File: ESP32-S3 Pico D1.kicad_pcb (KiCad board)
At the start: 6 copper layers, 31 x 30.5 mm, 55 parts, among them CN1 USC_C_Receptacle_Hirose_CX90M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, CN2 BM04B-ACHSS, CN3 Conn_Coaxial_Small, SW1 SPST-NO, SW2 SPST-NO, U1 TPSM82903, U2 TPS2117DRL, U3 TPS2117DRL, U4 NCP167, U5 ESP32-S3-PICO-1-N8R8, U6 BGS12WN6, U7 TCAN1057AVDRBRQ1, U8 74HCT00

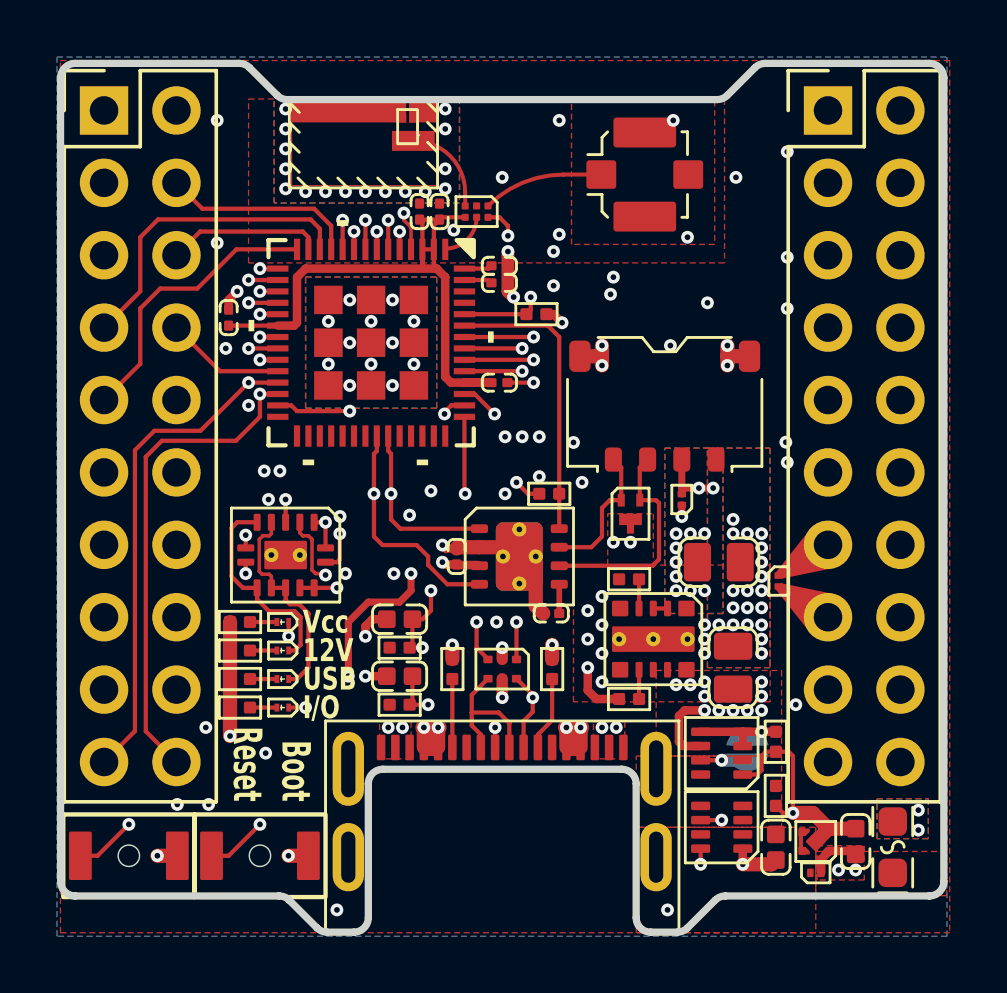
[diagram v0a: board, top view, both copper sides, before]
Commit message: successful 1st pass, but I want to try some new bus'ing techniques to clean up the routing
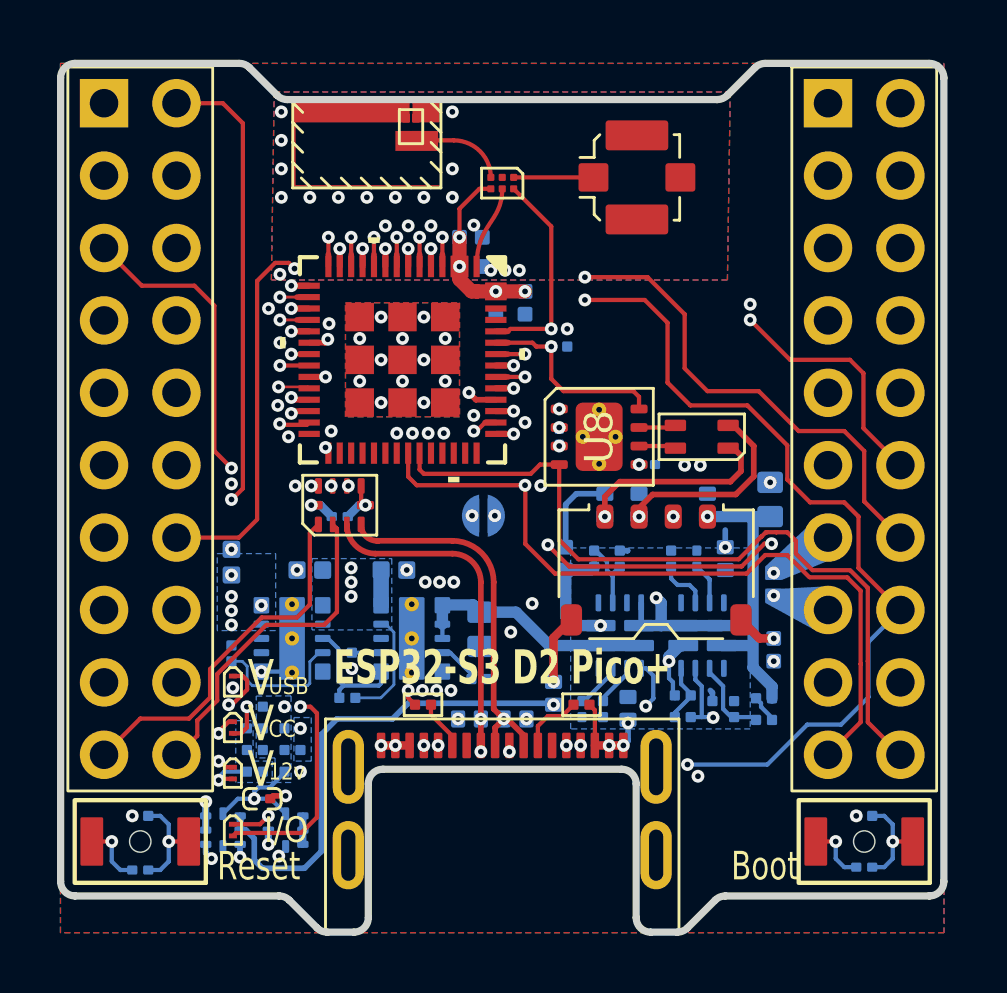
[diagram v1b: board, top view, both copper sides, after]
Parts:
- removed C13: 100n, Capacitors:C0201_Dense
- removed ESD1: PRTR5V0U2F, Personal_FootprintLibrary:XSON6
- removed ESD2: ESDCAN03-2BM3Y, Personal_FootprintLibrary:DFN1110-3
- removed ESD3: PESD5V0X1BCSF, Personal_FootprintLibrary:DSN0603-2
- removed ESD4: DESD18VF1BLP3-7, Personal_FootprintLibrary:DSN0603-2
- removed F1: 6V, 750mA, Personal_FootprintLibrary:Fuse_0603_1608Metric
- added C15: 1uF, Capacitors:C0201_Dense, B.Cu at (143.0, 114.8)
- added C16: 1uF, Capacitors:C0201_Dense, B.Cu at (156.8, 117.4)
- added C17: 22uF, Capacitors:C0402_Dense, B.Cu at (149.8, 108.4)
- added C18: 22uF, Capacitors:C0603_Dense, B.Cu at (159.4, 115.3)
- added C19: 22uF, Capacitors:C0402_Dense, B.Cu at (148.9, 106.1)
- added C20: 22uF, Capacitors:C0402_Dense, B.Cu at (152.2, 117.4)
- added C21: 22uF, Capacitors:C0402_Dense, B.Cu at (159.5, 120.6)
- added CMC1: CMC 0805, Personal_FootprintLibrary:CMC_0805, F.Cu at (157.0, 113.1)
- added D2: PESD24VF1BL-Q, Personal_FootprintLibrary:DFN1006-2, B.Cu at (148.8, 123.0)
- added D3: PESD24VF1BL-Q, Personal_FootprintLibrary:DFN1006-2, B.Cu at (150.4, 123.0)
- added D4: VESD16C1-HD1HG3-08, Personal_FootprintLibrary:DFN1006-2, B.Cu at (157.8, 117.4)
- added D5: VESD16C1-HD1HG3-08, Personal_FootprintLibrary:DFN1006-2, B.Cu at (159.5, 118.3)
- added D6: VESD16C1-HD1HG3-08, Personal_FootprintLibrary:DFN1006-2, B.Cu at (154.4, 122.6)
- added D7: PESD24VF1BL-Q, Personal_FootprintLibrary:DFN1006-2, B.Cu at (153.6, 115.5)
- added D8: PESD24VF1BL-Q, Personal_FootprintLibrary:DFN1006-2, B.Cu at (154.8, 115.5)
- added D9: VESD16C1-HD1HG3-08, Personal_FootprintLibrary:DFN1006-2, B.Cu at (157.2, 115.5)
- added R15: 40k2, Resistors:R0201_Dense, B.Cu at (155.9, 117.4)
- added R16: 95k3, Resistors:R0201_Dense, B.Cu at (156.3, 122.2)
- added R17: 95k3, Resistors:R0201_Dense, B.Cu at (156.3, 122.9)
- added R18: 40k2, Resistors:R0201_Dense, B.Cu at (159.2, 122.3)
- added R19: 5R1, Resistors:R0201_Dense, B.Cu at (159.2, 123.0)
- added R20: 5R1, Resistors:R0201_Dense, B.Cu at (158.1, 122.7)
- added R21: 95k3, Resistors:R0201_Dense, B.Cu at (157.4, 122.7)
- added R22: 95k3, Resistors:R0201_Dense, B.Cu at (142.6, 124.9)
- added R23: 5k1, Resistors:R0201_Dense, B.Cu at (142.6, 123.3)
- added R24: 1k, Resistors:R0201_Dense, B.Cu at (141.3, 123.3)
- added R25: 1k, Resistors:R0201_Dense, B.Cu at (141.3, 124.9)
- added R26: 95k3, Resistors:R0201_Dense, B.Cu at (153.2, 117.4)
- added R27: 40k2, Resistors:R0201_Dense, B.Cu at (153.5, 122.7)
- added R28: 40k2, Resistors:R0201_Dense, B.Cu at (154.1, 117.4)
- added U10: NC7WZ132L8X, Personal_FootprintLibrary:UQFN8_1.6x1.6mm_P0.5, B.Cu at (140.2, 126.9)
- added U9: TS3USB221A-Q1, Personal_FootprintLibrary:Texas_UQFN-10_1.5x2mm_P0.5mm, F.Cu at (144.3, 115.5)
- C1: value 22u -> 22uF; footprint Capacitors:C0805_Dense -> Capacitors:C0603_Dense; moved to B.Cu
- C10: value 100n -> 22uF; footprint Capacitors:C0201_Dense -> Capacitors:C0402_Nominal; moved to B.Cu
- C11, C12: value 1u -> 22uF; footprint Capacitors:C0402_Nominal -> Capacitors:C0402_Dense; moved to B.Cu
- C14, C5, C6, C8, C9: value 100n -> 1uF; moved to B.Cu
- C2: value 22u -> 22uF; footprint Capacitors:C0805_Dense -> Capacitors:C0402_Nominal; moved to B.Cu
- C3: value 1u -> 22uF; moved to B.Cu
- C4: value 1u -> 1uF; footprint Capacitors:C0402_Nominal -> Capacitors:C0201_Dense; moved to B.Cu
- C7: value 100n -> 1uF
- D1: value SDM02M30LP3-7B -> VESD16C1-HD1HG3-08; footprint Personal_FootprintLibrary:DSN0603-2 -> Personal_FootprintLibrary:DFN1006-2; moved to B.Cu
- H1, H2: value ~ -> ESP_Header
- R1, R9: value 26k1 -> 40k2; footprint Resistors:R0201_Nominal -> Resistors:R0201_Dense; moved to B.Cu
- R10, R11, R8: value 5R1 -> 1k; footprint Resistors:R0201_Nominal -> Resistors:R0201_Dense; moved to B.Cu
- R12, R13, R14, R2, R7: footprint Resistors:R0201_Nominal -> Resistors:R0201_Dense; moved to B.Cu
- R3: value 5R1 -> 40k2; footprint Resistors:R0201_Nominal -> Resistors:R0201_Dense; moved to B.Cu
- R4: value 5R1 -> 95k3; footprint Resistors:R0201_Nominal -> Resistors:R0201_Dense; moved to B.Cu
- R5, R6: footprint Resistors:R0201_Nominal -> Resistors:R0201_Dense
- U1: value TPSM82903 -> NC7WZ132L8X; footprint Personal_FootprintLibrary:uSIP-11_3.0x2.8 -> Personal_FootprintLibrary:UQFN8_1.6x1.6mm_P0.5; moved to B.Cu
- U2, U3: value TPS2117DRL -> TPS2121; footprint Personal_FootprintLibrary:SOT5x3 -> Personal_FootprintLibrary:VQHN-HR-12; moved to B.Cu
- U4: value NCP167 -> TPSM82903; footprint Personal_FootprintLibrary:XDFN4_1.0x1.0mm -> Personal_FootprintLibrary:uSIP-11_3.0x2.8_ThermalVias; moved to B.Cu
- U5: value ESP32-S3-PICO-1-N8R8 -> TPSM82903; footprint Personal_FootprintLibrary:ESP32-S3-Pico-1 -> Personal_FootprintLibrary:uSIP-11_3.0x2.8_ThermalVias; moved to B.Cu
- U6: value BGS12WN6 -> ESP32-S3-PICO-1-N8R8; footprint Personal_FootprintLibrary:TSNP-6 -> Personal_FootprintLibrary:ESP32-S3-Pico-1
- U7: value TCAN1057AVDRBRQ1 -> BGS12WN6; footprint Personal_FootprintLibrary:VSON-8-1EP_3x3mm_P0.65mm_EP1.65x2.4mm_ThermalVias -> Personal_FootprintLibrary:TSNP-6
- U8: value 74HCT00 -> TCAN1057AVDRBRQ1; footprint Personal_FootprintLibrary:WQFN-14-1EP_2.5x3mm_P0.5mm_EP1x1.5mm -> Personal_FootprintLibrary:VSON-8-1EP_3x3mm_P0.65mm_EP1.65x2.4mm_ThermalVias
- moved C8 24.1 mm to (137.3, 128.3), turned to 180 degrees
- moved C9 21.3 mm to (162.7, 128.2), turned to 180 degrees
- moved SW2 21.2 mm to (162.7, 127.3), turned to 180 degrees
- moved C7 20.5 mm to (141.6, 125.8)
- moved R3 19.3 mm to (140.5, 120.7)
- moved C6 18.4 mm to (152.8, 122.7), turned to -90 degrees
- moved C4 17.6 mm to (152.0, 113.1)
- moved R13 16.8 mm to (162.7, 126.4)
- moved C3 16.6 mm to (146.2, 117.8), turned to 0 degrees
- moved U4 15.9 mm to (146.8, 120.2), turned to -90 degrees
- moved R4 15.4 mm to (144.6, 122.3), turned to 180 degrees
- moved C2 15.2 mm to (143.2, 117.8), turned to 180 degrees
- moved U1 14.5 mm to (142.4, 126.9), turned to -90 degrees
- moved C12 13.8 mm to (150.8, 108.4), turned to -90 degrees
- moved U7 13.1 mm to (150.0, 104.2), turned to 180 degrees
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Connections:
- net /USB_Power_Interface/LED1_H renamed /User Interface/LED1_H
- net /USB_Power_Interface/LED3_H renamed /User Interface/LED3_H
- net /USB_Power_Interface/USB_CC2 renamed /USB_Power_Interface/CC2
- C1 pad 1: +12Vacc -> 2121b
- C11 pad 1: EN -> +3V3
- C12 pad 1: IO_00 -> +3V3
- C3 pad 1: +5V0 -> +5V1
- C4 pad 1: +3V3 -> +5V1
- C6 pad 1: +3V3 -> /USB_Power_Interface/SSb
- C6 pad 2: GND -> /USB_Power_Interface/GND1
- C7 pad 1: +3V3 -> +5V1
- C8 pad 1: +3V3 -> EN
- C9 pad 1: +3V3 -> IO_00
- CN1 pad A5: /USB_Power_Interface/USB_CC1 -> /USB_Power_Interface/CC1
- CN1 pad A6: /USB_Power_Interface/USBC_D+ -> USB_D+
- CN1 pad A7: /USB_Power_Interface/USBC_D- -> USB_D-
- CN1 pad B6: /USB_Power_Interface/USBC_D+ -> USB_D+
- CN1 pad B7: /USB_Power_Interface/USBC_D- -> USB_D-
- CN2 pad 1: GND -> /CAN_Interface/CAN-
- CN2 pad 2: +12Vacc -> /CAN_Interface/CAN+
- CN2 pad 3: CAN_L -> GND
- CN2 pad 4: CAN_H -> +16V
- D1 pad 1: +5V0 -> +VBus
- D1 pad 2: +3V3 -> GND
- H1 pad 10: USB_D- -> IO_20
- H1 pad 13: IO_08 -> IO_09
- H1 pad 20: USB_D+ -> IO_19
- H1 pad 5: IO_09 -> IO_08
- H1 pad 9: +5VF -> +5V1
- H2 pad 10: IO_47 -> IO_48
- H2 pad 20: IO_48 -> IO_47
- H2 pad 8: +5Vcc -> +5Vext
- JP1 pad 1: +5Vpri -> 2121a
- LED1 pad 1: /USB_Power_Interface/LED1_L -> /User Interface/LED1_L
- LED2 pad 1: /USB_Power_Interface/LED2_L -> /User Interface/LED2_L
- LED2 pad 2: /USB_Power_Interface/LED2_H -> /User Interface/LED2_H
- LED3 pad 1: /USB_Power_Interface/LED3_L -> /User Interface/LED3_L
- LED4 pad 1: LED4_L -> STb
- LED4 pad 2: Net-(LED4-A) -> /User Interface/LED4_H
- R1 pad 1: Net-(U1-S-CONF) -> /USB_Power_Interface/SCONFc
- R10 pad 2: +5VF -> +5V1
- R11 pad 1: Net-(LED4-A) -> /User Interface/LED4_SR
- R11 pad 2: +5VF -> +5V1
- R2 pad 1: Net-(U1-FB/VSET) -> /USB_Power_Interface/VSETc
- R3 pad 1: GND -> /USB_Power_Interface/SCONFd
- R3 pad 2: +VBus -> GND
- R4 pad 1: GND -> +5V1
- R4 pad 2: +5Vpri -> /USB_Power_Interface/PG_EN
- R5 pad 1: /USB_Power_Interface/USB_CC1 -> GND
- R5 pad 2: GND -> /USB_Power_Interface/CC1
- R7 pad 2: Ant_Sel -> /ESP32-S3-PICO-1/Ant_Sel
- R8 pad 2: +5VF -> +5V1
- R9 pad 1: +5VF -> +5V1
- R9 pad 2: unconnected-(R9-Pad2) -> /User Interface/LED2_H
- U1 pad 1: +12Vacc -> Net-(U1-Pad1)
- U1 pad 2: +12Vacc -> Net-(U1-Pad1)
- U1 pad 3: +12Vacc -> Net-(U1-Pad1)
- U1 pad 4: Net-(U1-S-CONF) -> GND
- U1 pad 5: unconnected-(U1-SS/TR-Pad5) -> IO_02
- U1 pad 6: unconnected-(U1-PG-Pad6) -> IO_02
- U1 pad 7: Net-(U1-FB/VSET) -> /User Interface/LED1_L
- U1 pad 8: unconnected-(U1-SW-Pad8) -> +5V1
- U2 pad 1: GND -> 2121a
- U2 pad 2: +5Vpri -> +16V
- U2 pad 3: +VBus -> /USB_Power_Interface/GND1
- U2 pad 4: +VBus -> /USB_Power_Interface/OV2a
- U2 pad 5: +VBus -> OV1a
- U2 pad 6: +5V1 -> /USB_Power_Interface/PR1a
- U2 pad 7: +5Vpri -> +VBus
- U2 pad 8: unconnected-(U2-ST-Pad8) -> 2121a
- U3 pad 1: GND -> 2121b
- U3 pad 2: +5V0 -> +5Vext
- U3 pad 3: +5Vpri -> /USB_Power_Interface/GND1
- U3 pad 4: +5Vpri -> /USB_Power_Interface/OV2b
- U3 pad 5: +5Vpri -> /USB_Power_Interface/GND1
- U3 pad 6: +5Vcc -> 2121a
- U3 pad 7: +5V0 -> 2121a
- U3 pad 8: GND -> 2121b
- U4 pad 1: +3V3 -> 2121b
- U4 pad 2: GND -> 2121b
- U4 pad 3: +5V0 -> 2121b
- U4 pad 4: +5V0 -> /USB_Power_Interface/SCONFc
- U5 pad 1: RFIN -> +5V1
- U5 pad 10: IO_05 -> +3V3
- U5 pad 11: IO_06 -> GND
- U5 pad 2: +3V3 -> +5V1
- U5 pad 3: +3V3 -> /USB_Power_Interface/PG_EN
- U5 pad 4: EN -> /USB_Power_Interface/SCONFd
- U5 pad 5: IO_00 -> unconnected-(U5-SS/TR-Pad5)
- U5 pad 6: IO_01 -> GND
- U5 pad 7: IO_02 -> unconnected-(U5-FB/VSET-Pad7)
- U5 pad 8: IO_03 -> unconnected-(U5-SW-Pad8)
- U5 pad 9: IO_04 -> +3V3
- U6 pad 1: /ESP32-S3-PICO-1/RF2 -> /ESP32-S3-PICO-1/RF_In
- U6 pad 2: GND -> +3V3
- U6 pad 3: /ESP32-S3-PICO-1/RF1 -> +3V3
- U6 pad 4: +3V3 -> EN
- U6 pad 5: RFIN -> IO_00
- U6 pad 6: Ant_Sel -> IO_01
- U7 pad 1: IO_47 -> /ESP32-S3-PICO-1/RF2
- U7 pad 3: +5VF -> /ESP32-S3-PICO-1/RF1
- U7 pad 4: IO_48 -> +3V3
- U7 pad 5: +3V3 -> /ESP32-S3-PICO-1/RF_In
- U7 pad 6: CAN_L -> /ESP32-S3-PICO-1/Ant_Sel
- U8 pad 1: IO_02 -> IO_48
- U8 pad 2: IO_02 -> GND
- U8 pad 3: /USB_Power_Interface/LED1_L -> +5V1
- U8 pad 4: +5Vpri -> IO_47
- U8 pad 5: /USB_Power_Interface/LED2_L -> +3V3
- U8 pad 6: LED4_L -> /CAN_Interface/CAN_L_F
- U8 pad 7: GND -> /CAN_Interface/CAN_H_F
- U8 pad 8: /USB_Power_Interface/LED3_L -> CAN_S
- U8 pad 9: LED4_L -> GND
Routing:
- net +5VF: track 72.3 -> 0.00 mm, vias 7 -> 0
- net +3V3: track 29.1 -> 83.2 mm, vias 15 -> 16
- net GND: track 33.1 -> 70.8 mm, vias 107 -> 82
- net +5V1: track 2.70 -> 33.5 mm, vias 11 -> 6
- net USB_D-: track 37.8 -> 12.6 mm, vias 2 -> 1
- net +5Vpri: track 25.1 -> 0.00 mm, vias 3 -> 0
- net STb: track 0.00 -> 24.4 mm, vias 0 -> 4
- net USB_D+: track 35.7 -> 11.7 mm, vias 2 -> 3
- net OV1a: track 0.00 -> 22.3 mm, vias 0 -> 2
- net IO_00: track 60.7 -> 39.0 mm, vias 5 -> 3
- net IO_02: track 45.6 -> 59.3 mm, vias 3 -> 4
- net IO_20: track 0.00 -> 12.9 mm
- net 2121a: track 0.00 -> 12.3 mm, vias 0 -> 2
- net IO_19: track 0.00 -> 11.7 mm
- net +5Vext: track 0.00 -> 10.5 mm, vias 0 -> 2
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- added copper zone on B.Cu, net +3V3
- added copper zone on B.Cu, net +5V1
- added copper zone on B.Cu, net /USB_Power_Interface/GND1
- added copper zone on B.Cu, net /User Interface/LED2_H
- added copper zone on B.Cu, net /User Interface/LED4_SR
- removed copper zone on B.Cu, net +12Vacc
- removed copper zone on F.Cu, net +12Vacc
- removed copper zone on In1.Cu, net +12Vacc
- removed copper zone on In2.Cu, net +12Vacc
- removed copper zone on In3.Cu, net +12Vacc
- removed copper zone on In4.Cu, net +12Vacc
- removed copper zone on F.Cu, net +3V3
- removed copper zone on In2.Cu, net +3V3
- removed copper zone on In4.Cu, net +3V3
- removed copper zone on F.Cu, net +5V0
- removed copper zone on F.Cu, net +5V1
- removed copper zone on In2.Cu, net +5V1
- removed copper zone on In4.Cu, net +5V1
- removed copper zone on B.Cu, net +5VF
- removed copper zone on F.Cu, net +5VF
- removed copper zone on In1.Cu, net +5VF
- removed copper zone on In2.Cu, net +5VF
- removed copper zone on In3.Cu, net +5VF
- removed copper zone on In4.Cu, net +5VF
- removed copper zone on F.Cu, net +5Vpri
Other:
- board text added: "12v"
- board text added: "CC"
- board text added: "ESP32-S3 D2 Pico+"
- board text added: "RHK ESP32-S3 D2 Pico+"
- board text added: "V"
- board text added: "©2026"
- board text removed: "12V"
- board text removed: "JLCJLCJLCJLC"
- board text removed: "Vcc"

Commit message: Update CAN_Interface.kicad_sch, ESP32-S3 Pico D1.kicad_dru, ESP32-S3 Pico D1.kicad_pcb, and 5 more files reroute completed
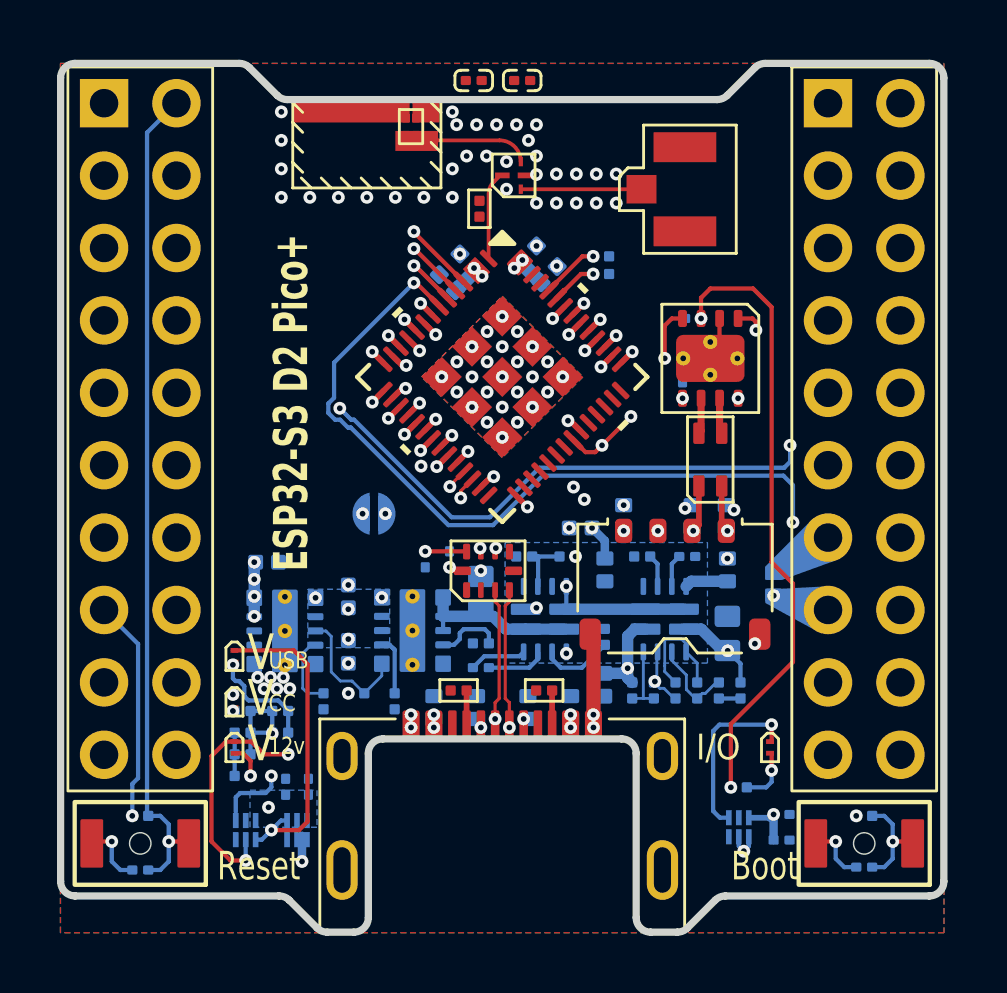
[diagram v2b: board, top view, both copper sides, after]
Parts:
- removed C7: 1uF, Capacitors:C0201_Dense
- removed R25: 1k, Resistors:R0201_Dense
- removed U10: NC7WZ132L8X, Personal_FootprintLibrary:UQFN8_1.6x1.6mm_P0.5
- removed U7: BGS12WN6, Personal_FootprintLibrary:TSNP-6
- added C22: 100nF, Capacitors:C0201_Dense, B.Cu at (159.8, 127.2)
- added C23: 1uF, Capacitors:C0201_Dense, B.Cu at (143.2, 125.4)
- added C24: 100nF, Capacitors:C0201_Dense, B.Cu at (159.8, 126.3)
- added C26: 1uF, Capacitors:C0201_Dense, B.Cu at (142.4, 125.4)
- added C28: DNP, Capacitors:C0201_Dense, F.Cu at (150.7, 100.6)
- added C29: DNP, Capacitors:C0201_Dense, F.Cu at (149.0, 100.6)
- added D10: D15V0H1U2LP-7B, Personal_FootprintLibrary:DFN1006-2, B.Cu at (147.6, 122.6)
- added R30: 0R, Resistors:R0201_Dense, F.Cu at (149.2, 105.1)
- added U11: 74LVC1G38, Personal_FootprintLibrary:DSF6, B.Cu at (158.3, 126.8)
- added U12: 74LVC1G38, Personal_FootprintLibrary:DSF6, B.Cu at (142.8, 126.9)
- added U13: 74LVC1G38, Personal_FootprintLibrary:DSF6, B.Cu at (141.0, 126.9)
- C10, C2, C3: footprint Capacitors:C0402_Nominal -> Capacitors:C0402_Dense
- CN1: value USC_C_Receptacle_Hirose_CX90M-16P -> GT-USB-7014D; footprint Personal_FootprintLibrary:USB_C_Receptacle_Hirose_CX90M-16P -> Personal_FootprintLibrary:USB_C_Receptacle_G-Switch-GT-USB-7014D
- CN3: value Conn_Coaxial_Small -> 2337019-1; footprint Personal_FootprintLibrary:U.FL_Molex_MCRF_73412 -> Personal_FootprintLibrary:u.FL_Male_Pin_Coax_SMD
- D1, D4, D5, D6, D9: value VESD16C1-HD1HG3-08 -> D15V0H1U2LP-7B
- D2, D3, D7, D8: value PESD24VF1BL-Q -> ESDSLC24VLB-TP
- R12, R13, R19, R20, R5, R6: value 5R1 -> 5k1
- R14, R7: value 5R1 -> 95k3
- R22: value 95k3 -> 1k
- U1: value NC7WZ132L8X -> SKYA21024; footprint Personal_FootprintLibrary:UQFN8_1.6x1.6mm_P0.5 -> Personal_FootprintLibrary:SKYA21024; moved to F.Cu
- U6: value ESP32-S3-PICO-1-N8R8 -> ESP32-S3-PICO-1-N8R2
- moved R12 25.4 mm to (162.7, 126.4)
- moved R13 25.4 mm to (137.3, 126.4)
- moved U1 24.3 mm to (150.4, 103.9), turned to 0 degrees
- moved LED1 19.1 mm to (159.4, 124.0)
- moved R8 15.9 mm to (158.3, 125.4)
- moved C4 6.27 mm to (156.7, 109.0), turned to 180 degrees
- moved C21 6.05 mm to (153.6, 121.8), turned to -90 degrees
- moved U9 5.69 mm to (149.5, 117.8)
- moved C15 4.99 mm to (147.3, 117.4), turned to -90 degrees
- moved C18 4.93 mm to (157.9, 120.0)
- moved D6 4.93 mm to (153.6, 117.8), turned to -90 degrees
- moved U8 4.77 mm to (157.3, 110.3), turned to 180 degrees
- moved R6 4.34 mm to (148.5, 122.0)
- moved R5 4.28 mm to (151.5, 122.0)
- moved C14 4.13 mm to (148.2, 117.4), turned to 90 degrees
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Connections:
- net /CAN_Interface/CAN_H_F renamed /CAN_Interface/CAN_F_P
- net /CAN_Interface/CAN_L_F renamed /CAN_Interface/CAN_F_N
- ANT1 pad 1: /ESP32-S3-PICO-1/RF1 -> /ESP32-S3-PICO-1/RF2
- ANT1 pad 4: /ESP32-S3-PICO-1/RF1 -> /ESP32-S3-PICO-1/RF2
- CMC1 pad 1: /CAN_Interface/CAN- -> /CAN_Interface/CAN_N
- CMC1 pad 2: /CAN_Interface/CAN+ -> /CAN_Interface/CAN_P
- CN2 pad 1: /CAN_Interface/CAN- -> +16V
- CN2 pad 2: /CAN_Interface/CAN+ -> GND
- CN2 pad 3: GND -> /CAN_Interface/CAN_N
- CN2 pad 4: +16V -> /CAN_Interface/CAN_P
- CN3 pad 1: /ESP32-S3-PICO-1/RF2 -> /ESP32-S3-PICO-1/RF1
- D2 pad 1: GND -> USB_D+
- D2 pad 2: USB_D+ -> GND
- D3 pad 1: GND -> USB_D-
- D3 pad 2: USB_D- -> GND
- D7 pad 1: /CAN_Interface/CAN- -> /CAN_Interface/CAN_N
- D8 pad 1: /CAN_Interface/CAN+ -> /CAN_Interface/CAN_P
- H1 pad 10: IO_20 -> IO_10
- H1 pad 12: IO_06 -> IO_00
- H1 pad 13: IO_09 -> IO_02
- H1 pad 14: IO_18 -> IO_05
- H1 pad 15: IO_11 -> IO_07
- H1 pad 16: IO_38 -> IO_06
- H1 pad 17: IO_05 -> IO_11
- H1 pad 20: IO_19 -> IO_12
- H1 pad 3: IO_39 -> IO_01
- H1 pad 4: IO_07 -> IO_03
- H1 pad 5: IO_08 -> IO_04
- H1 pad 6: IO_10 -> IO_09
- H1 pad 7: IO_14 -> IO_08
- H2 pad 1: IO_01 -> unconnected-(H2-Pin_1-Pad1)
- H2 pad 10: IO_48 -> IO_17
- H2 pad 15: IO_12 -> IO_39
- H2 pad 16: IO_04 -> IO_47
- H2 pad 17: IO_00 -> IO_48
- H2 pad 18: IO_02 -> IO_18
- H2 pad 19: IO_40 -> IO_14
- H2 pad 2: IO_03 -> CAN_Silent
- H2 pad 20: IO_47 -> IO_15
- H2 pad 4: IO_21 -> IO_40
- H2 pad 5: IO_17 -> IO_38
- H2 pad 9: IO_15 -> IO_21
- R1 pad 1: /USB_Power_Interface/SCONFc -> GND
- R1 pad 2: GND -> /USB_Power_Interface/SCONFc
- R12 pad 1: EN -> IO_00
- R13 pad 1: IO_00 -> EN
- R14 pad 2: CAN_S -> CAN_Silent
- R15 pad 1: /USB_Power_Interface/ILMa -> /USB_Power_Interface/GND1
- R15 pad 2: /USB_Power_Interface/GND1 -> /USB_Power_Interface/ILMa
- R18 pad 1: +16V -> Net-(R18-Pad1)
- R18 pad 2: Net-(R18-Pad2) -> +16V
- R19 pad 2: Net-(R18-Pad2) -> Net-(R18-Pad1)
- R22 pad 1: STb -> /User Interface/LED4_SR
- R23 pad 1: +5V1 -> /User Interface/LED2_H
- R23 pad 2: /User Interface/LED2_H -> +5V1
- R24 pad 1: /User Interface/LED4_SR -> /User Interface/LED4_H
- R24 pad 2: +5V1 -> /User Interface/LED4_SR
- R27 pad 1: /USB_Power_Interface/ILMb -> /USB_Power_Interface/GND1
- R27 pad 2: /USB_Power_Interface/GND1 -> /USB_Power_Interface/ILMb
- R3 pad 1: /USB_Power_Interface/SCONFd -> GND
- R3 pad 2: GND -> /USB_Power_Interface/SCONFd
- R5 pad 2: /USB_Power_Interface/CC1 -> /USB_Power_Interface/CC2
- R6 pad 1: /USB_Power_Interface/CC2 -> GND
- R6 pad 2: GND -> /USB_Power_Interface/CC1
- R7 pad 2: /ESP32-S3-PICO-1/Ant_Sel -> /ESP32-S3-PICO-1/Ant_Select
- R9 pad 1: +5V1 -> /User Interface/LED2_H
- R9 pad 2: /User Interface/LED2_H -> +5V1
- U1 pad 1: Net-(U1-Pad1) -> +3V3
- U1 pad 2: Net-(U1-Pad1) -> /ESP32-S3-PICO-1/RF1
- U1 pad 3: Net-(U1-Pad1) -> GND
- U1 pad 4: GND -> /ESP32-S3-PICO-1/RF2
- U1 pad 5: IO_02 -> /ESP32-S3-PICO-1/Ant_Select
- U1 pad 6: IO_02 -> /ESP32-S3-PICO-1/RFC
- U6 pad 38: unconnected-(U6-GPIO33-Pad38) -> IO_33
- U6 pad 39: unconnected-(U6-GPIO34-Pad39) -> IO_34
- U6 pad 40: unconnected-(U6-GPIO35-Pad40) -> IO_35
- U6 pad 41: unconnected-(U6-GPIO36-Pad41) -> IO_36
- U6 pad 42: unconnected-(U6-GPIO37-Pad42) -> IO_37
- U6 pad 51: CAN_S -> CAN_Silent
- U6 pad 52: /ESP32-S3-PICO-1/Ant_Sel -> /ESP32-S3-PICO-1/Ant_Select
- U8 pad 8: CAN_S -> CAN_Silent
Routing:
- net +5V1: track 33.5 -> 58.5 mm, vias 6 -> 8
- net +3V3: track 83.2 -> 60.8 mm, vias 16 -> 18
- net CAN_Silent: track 0.00 -> 22.3 mm, vias 0 -> 2
- net IO_00: track 39.0 -> 60.3 mm, vias 3 -> 4
- net GND: track 70.8 -> 87.3 mm
- net +VBus: track 45.5 -> 30.8 mm, vias 8 -> 7
- net IO_18: track 6.29 -> 19.6 mm
- net IO_40: track 22.5 -> 9.42 mm
- net IO_20: track 12.9 -> 0.00 mm
- net IO_19: track 11.7 -> 0.00 mm
- net IO_12: track 31.1 -> 19.4 mm, vias 2 -> 1
- net IO_21: track 29.2 -> 18.0 mm
- net IO_39: track 24.4 -> 13.9 mm, vias 2 -> 1
- net IO_10: track 11.3 -> 21.2 mm
- net IO_04: track 23.0 -> 13.4 mm, vias 2 -> 1
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- added copper zone on In4.Cu, net +3V3
- added copper zone on In4.Cu, net +5V1
- added copper zone on In1.Cu, net /USB_Power_Interface/GND1
- added copper zone on In2.Cu, net /USB_Power_Interface/GND1
- added copper zone on In3.Cu, net /USB_Power_Interface/GND1
- added copper zone on In4.Cu, net /USB_Power_Interface/GND1
- removed copper zone on B.Cu, net /User Interface/LED2_H
- removed copper zone on B.Cu, net /User Interface/LED4_SR
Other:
- outline, holes or cut-outs redrawn
